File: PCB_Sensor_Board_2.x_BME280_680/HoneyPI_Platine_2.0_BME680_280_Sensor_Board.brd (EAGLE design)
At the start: 30 x 62 mm, 8 parts

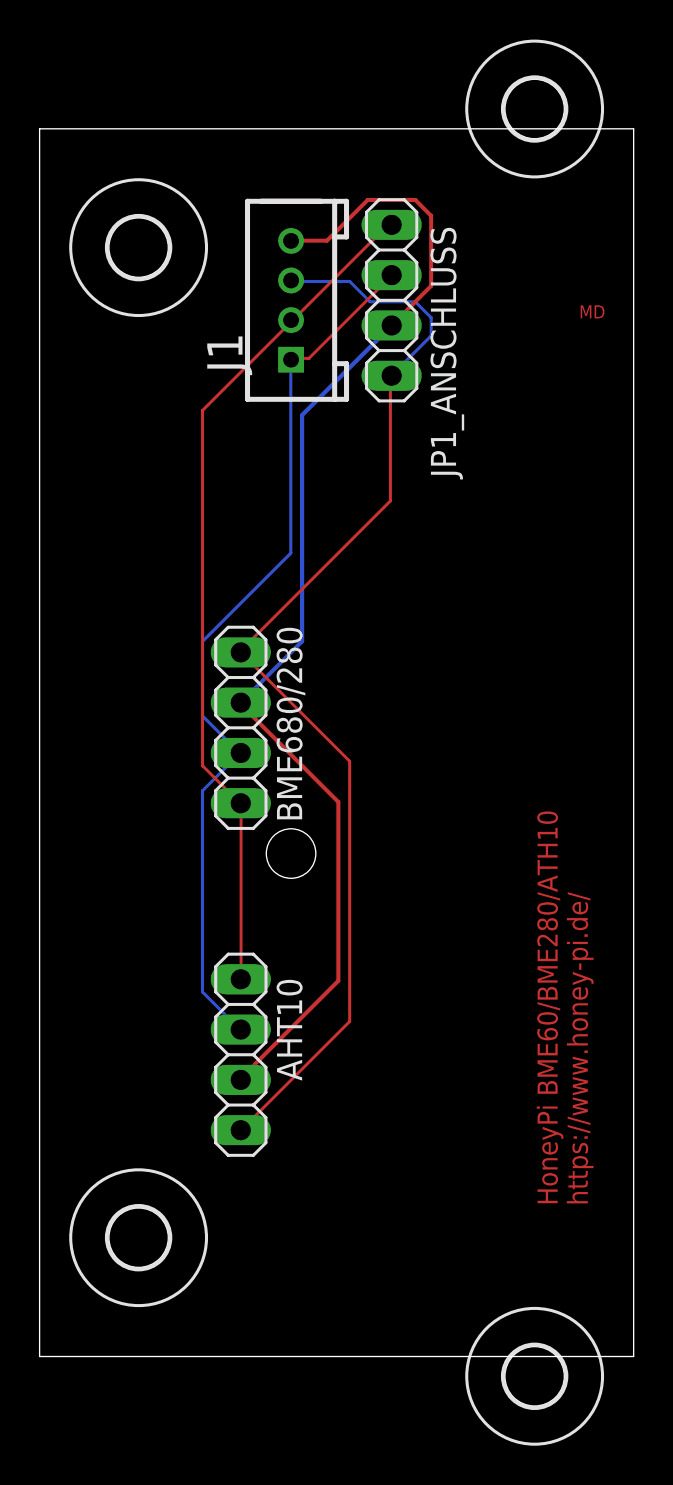
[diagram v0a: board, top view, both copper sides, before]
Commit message: 3rd i²C interface
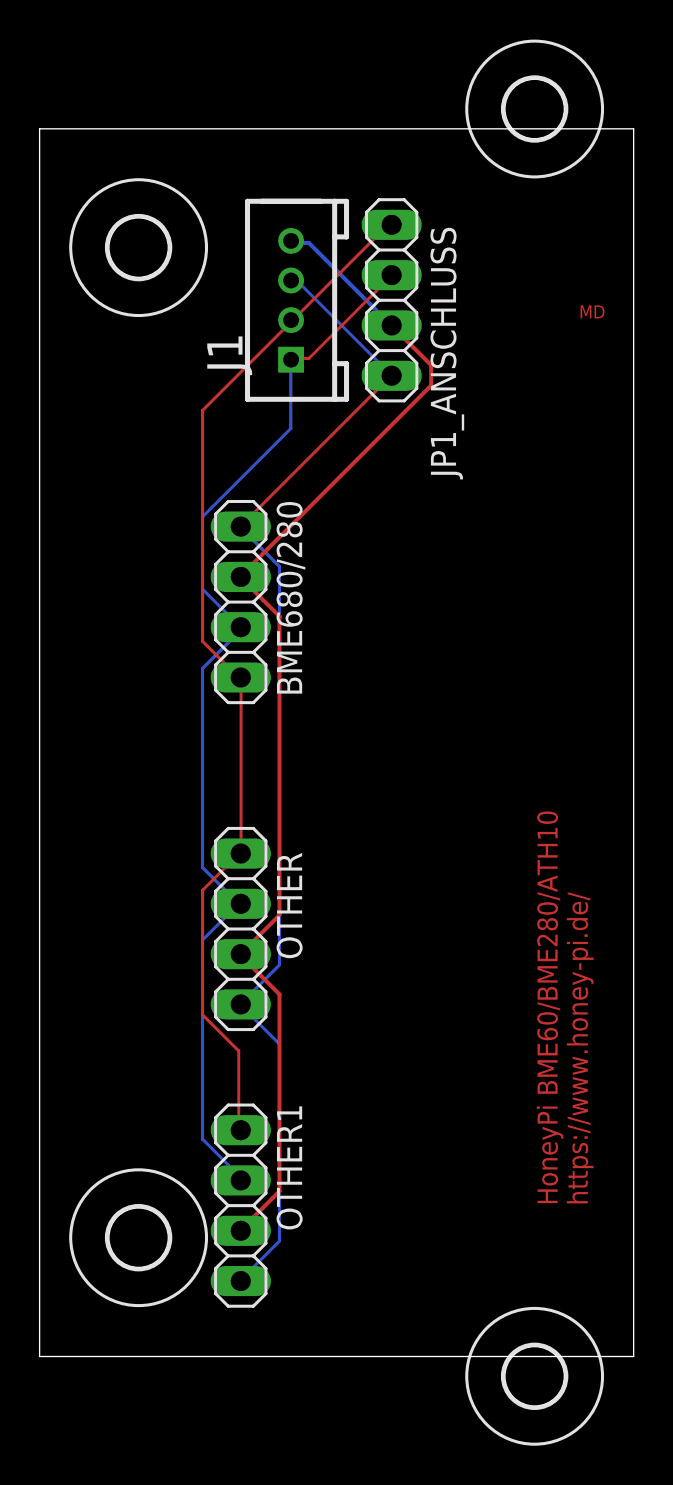
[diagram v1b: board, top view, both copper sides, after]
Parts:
- removed AHT10: (no value), pinhead:1X04
- added OTHER, OTHER1: (no value), pinhead:1X04
- moved BME680/280 6.35 mm to (10.2, 38.1)
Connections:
- net 3V3: now also OTHER.4, OTHER1.4; no longer AHT10.4
- net BME_SCL/SCK: now also OTHER.2, OTHER1.2; no longer AHT10.2
- net BME_SDI/SDA: now also OTHER.1, OTHER1.1; no longer AHT10.1
- net GND: now also OTHER.3, OTHER1.3; no longer AHT10.3
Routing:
- net BME_SDI/SDA: track 43.0 -> 52.4 mm
- net BME_SCL/SCK: track 45.0 -> 54.2 mm
- net 3V3: track 57.4 -> 59.2 mm
- net GND: track 60.0 -> 60.6 mm

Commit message: Updates, updates...
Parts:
- added GND: (no value), pinhead:1X04
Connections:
- net GND: now also GND.1, GND.2, GND.3, GND.4
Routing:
- net GND: track 60.6 -> 70.1 mm
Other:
- board text added: "HoneyPI_Platine_2.0_BME680_280_Sensor_Board https://www.honey-pi.de/"
- board text removed: "HoneyPi BME60/BME280/ATH10 https://www.honey-pi.de/"
